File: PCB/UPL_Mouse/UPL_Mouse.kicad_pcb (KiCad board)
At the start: 2 copper layers, 32 x 32 mm, 10 parts, among them J1 PS2_5749180-1, J2 DB9_Female, J3 USB Micro_10118193-0001LF, J4 AVR-ISP-6, U1 MAX232DR, U2 ATTINY85

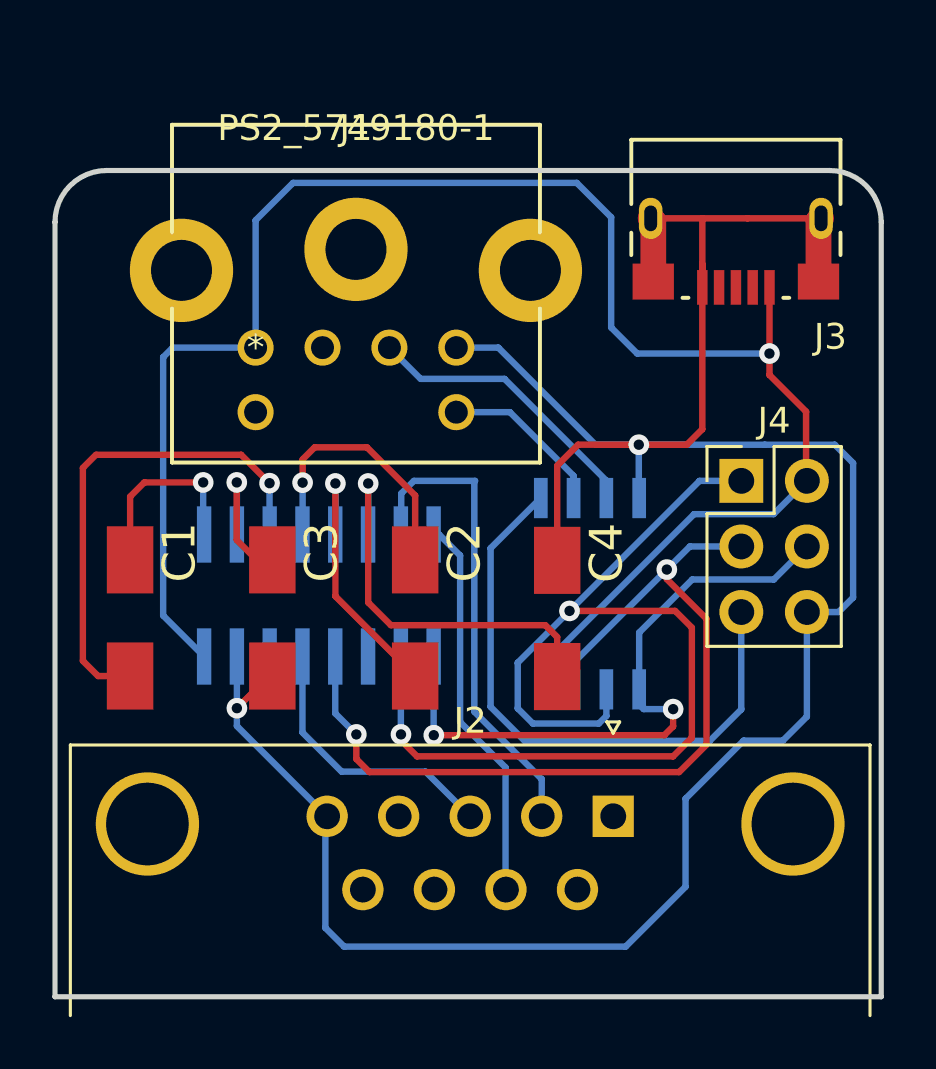
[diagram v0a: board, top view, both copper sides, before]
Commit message: Update Design and Code
Update in code regarding configuration of the chip.

Update in PCB due to wrong footprint mini din connector.
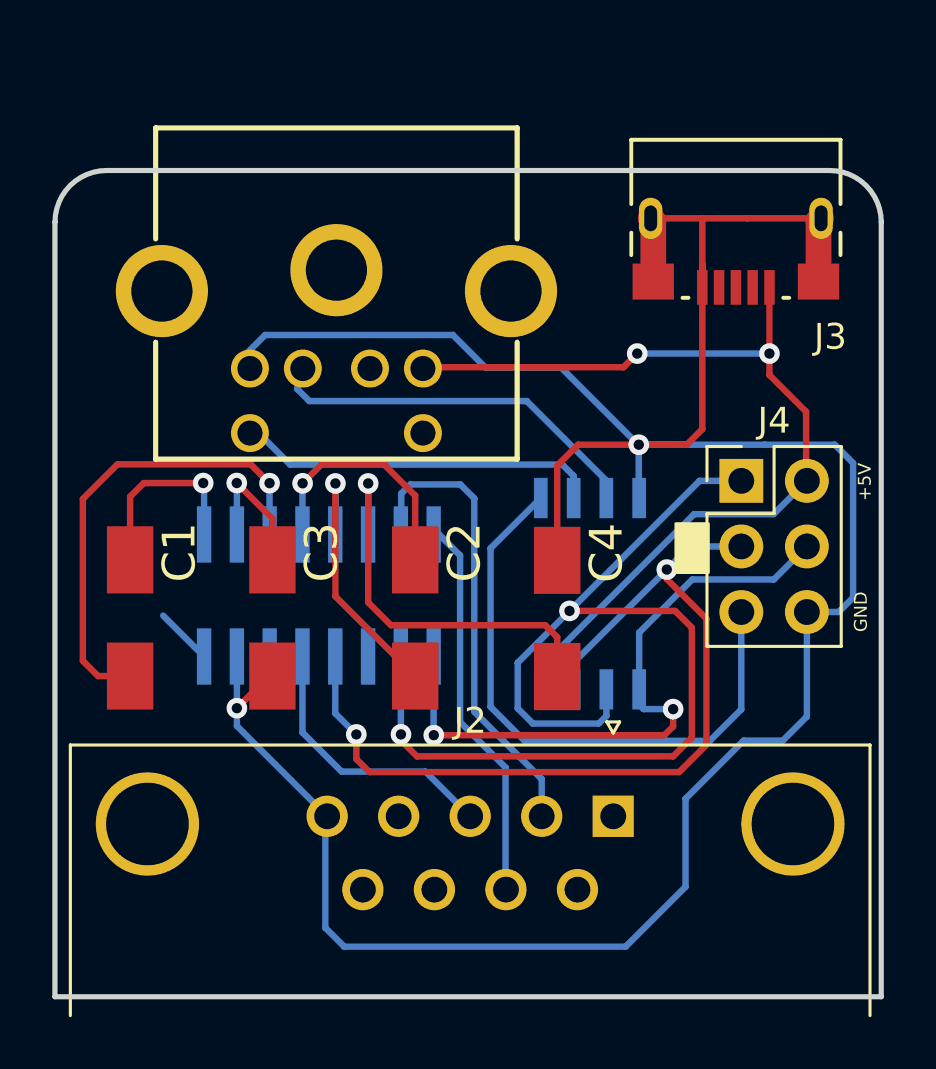
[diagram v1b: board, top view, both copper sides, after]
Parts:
- J1: moved to B.Cu
- U2: value ATTINY85 -> ATTINY85-20SH
- moved J1 9.07 mm to (126.0, 96.6), turned to 180 degrees
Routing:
- net VCC: track 68.9 -> 38.4 mm, vias 1 -> 2
- net GND: track 100.0 -> 109.3 mm
- net Net-(J1-Pad5): track 6.42 -> 14.2 mm
- net Net-(J1-Pad1): track 11.2 -> 14.8 mm
- net (no net): track 2.30 -> 0.00 mm
- net Net-(C2-Pad1): track 10.7 -> 9.63 mm
- net Net-(C1-Pad2): track 19.4 -> 18.4 mm
- net Net-(J2-Pad2): track 18.7 -> 18.2 mm
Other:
- board text added: "+5V"
- board text added: "BVKSound Mouse PS2 Serial 2021-04 Rev2"
- board text added: "GND"
- board text removed: "BVKSound Mouse PS2 Serial 2021-03"

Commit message: update with attiny84
update with attiny84 and rx tx
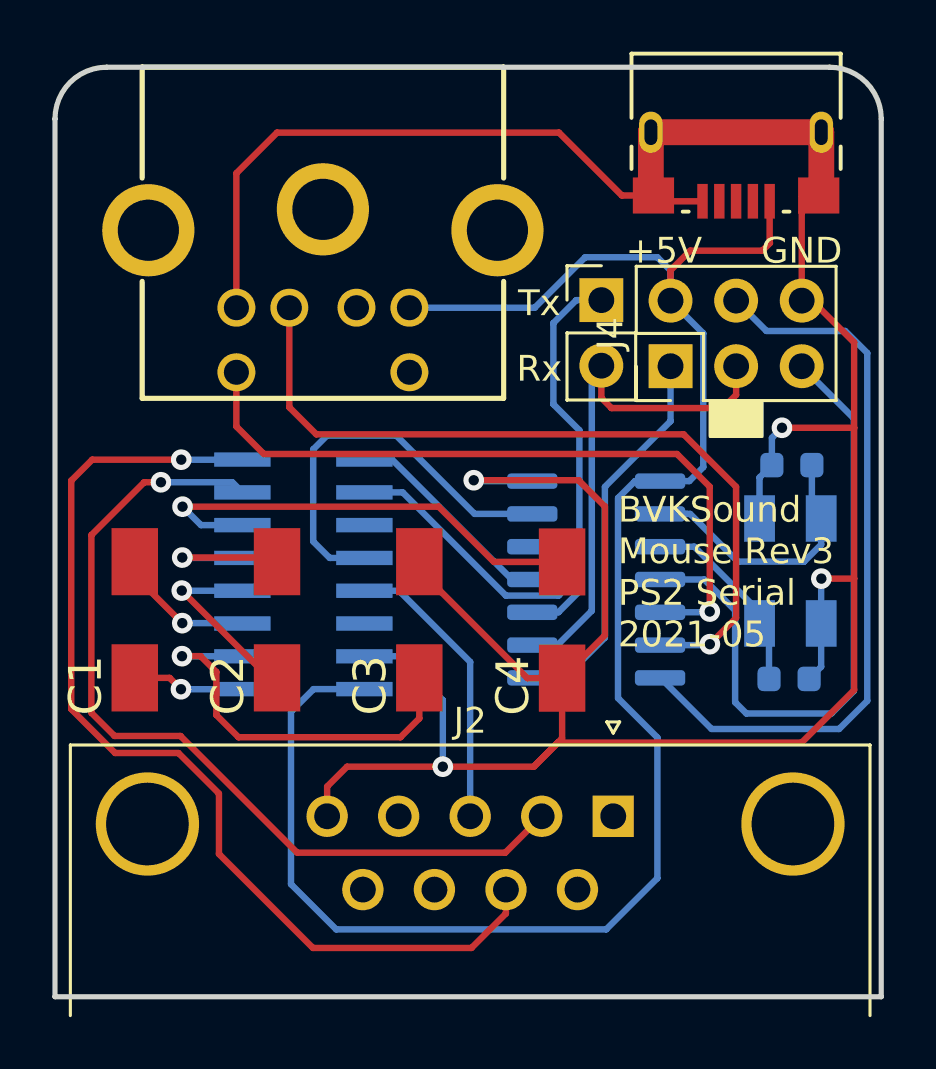
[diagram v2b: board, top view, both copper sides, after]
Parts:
- added C5: 22nF, Capacitor_SMD:C_0603_1608Metric, B.Cu at (143.6, 109.7)
- added C6: 22nF, Capacitor_SMD:C_0603_1608Metric, B.Cu at (143.5, 117.9)
- added J5: Conn_01x02_Male, Connector_PinHeader_2.54mm:PinHeader_1x02_P2.54mm_Vertical, F.Cu at (136.3, 103.3)
- added Y1: ABM3B-20.000MHZ, BVKSound:ABM3B-20.000MHZ, B.Cu at (143.6, 113.8)
- U2: value ATTINY85-20SH -> ATtiny84-20SSU; footprint BVKSound:ATTINY85-20SH -> Package_SO:SOIC-14_3.9x8.7mm_P1.27mm
- moved C3 5.69 mm to (129.2, 115.6), turned to 90 degrees
- moved C2 5.35 mm to (123.7, 115.6), turned to 90 degrees
- moved J4 5.22 mm to (138.9, 105.8), turned to 90 degrees
- moved J3 3.34 mm to (141.5, 96.8)
- moved J1 2.41 mm to (125.5, 94.2)
- moved U1 1.02 mm to (124.7, 113.9), turned to 0 degrees
- moved U2 0.60 mm to (136.1, 114.1), turned to 180 degrees
- moved C4 0.20 mm to (134.7, 115.7), turned to 90 degrees
- moved C1 0.19 mm to (118.2, 115.6), turned to 90 degrees
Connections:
- U1 pad 10: Net-(J4-Pad1) -> Net-(U1-Pad10)
- U1 pad 12: Net-(J4-Pad3) -> Net-(U1-Pad12)
- U1 pad 9: Net-(J4-Pad4) -> Net-(U1-Pad9)
- U2 pad 1: Net-(J4-Pad5) -> VCC
- U2 pad 2: Net-(J1-Pad5) -> Net-(C5-Pad1)
- U2 pad 3: Net-(J1-Pad1) -> Net-(C6-Pad1)
- U2 pad 4: GND -> Net-(J4-Pad5)
- U2 pad 5: Net-(J4-Pad4) -> Net-(J1-Pad5)
- U2 pad 6: Net-(J4-Pad1) -> Net-(J1-Pad1)
- U2 pad 7: Net-(J4-Pad3) -> Net-(J4-Pad4)
- U2 pad 8: VCC -> Net-(J4-Pad1)
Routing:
- net VCC: track 38.4 -> 71.1 mm, vias 2 -> 0
- net Net-(J4-Pad1): track 42.5 -> 15.0 mm, vias 2 -> 0
- net Net-(J2-Pad7): track 15.0 -> 39.3 mm, vias 0 -> 1
- net GND: track 109.3 -> 126.1 mm, vias 2 -> 4
- net Net-(J1-Pad1): track 14.8 -> 30.9 mm, vias 0 -> 1
- net Net-(J2-Pad2): track 18.2 -> 34.0 mm, vias 0 -> 1
- net Net-(U1-Pad12): track 0.00 -> 15.8 mm
- net Net-(J5-Pad1): track 0.00 -> 15.2 mm
- net Net-(J4-Pad3): track 35.3 -> 20.5 mm, vias 2 -> 0
- net Net-(J1-Pad5): track 14.2 -> 28.2 mm, vias 0 -> 1
- net Net-(C1-Pad2): track 18.4 -> 5.48 mm
- net Net-(U1-Pad10): track 0.00 -> 12.4 mm
- net Net-(C5-Pad1): track 0.00 -> 11.6 mm
- net Net-(C3-Pad1): track 5.54 -> 15.7 mm
- net Net-(C6-Pad1): track 0.00 -> 8.53 mm
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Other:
- board size 32 x 32 mm -> 32 x 36 mm
- board text added: "BVKSound Mouse Rev3 PS2 Serial 2021-05"
- board text added: "Rx"
- board text added: "Tx"
- board text removed: "BVKSound Mouse PS2 Serial 2021-04 Rev2"

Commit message: gerber files and cleanup pcb
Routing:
- net Net-(J2-Pad7): track 39.3 -> 38.0 mm
- net Net-(C4-Pad2): track 18.2 -> 19.1 mm
- net Net-(C2-Pad1): track 7.44 -> 8.28 mm
